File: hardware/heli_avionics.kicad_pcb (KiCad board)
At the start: 2 copper layers, 69 x 81.3 mm, 20 parts, among them J1 Pin_Header_2x3, J2 JST_PH_01x02, J3 JST_XH_01x02, J4 JST_XH_01x02, J5 JST_PH_01x03, J6 Battery JST, J7 JST_ZH_01x02, Q1 AO3400A, SW1 Reset, U1 ATmega4808-A, U2 nRF24L01P, U3 DRV8212, U4 DRV8212, U5 BMP390L, U6 TPS7A2030PDBV, Y1 16MHz

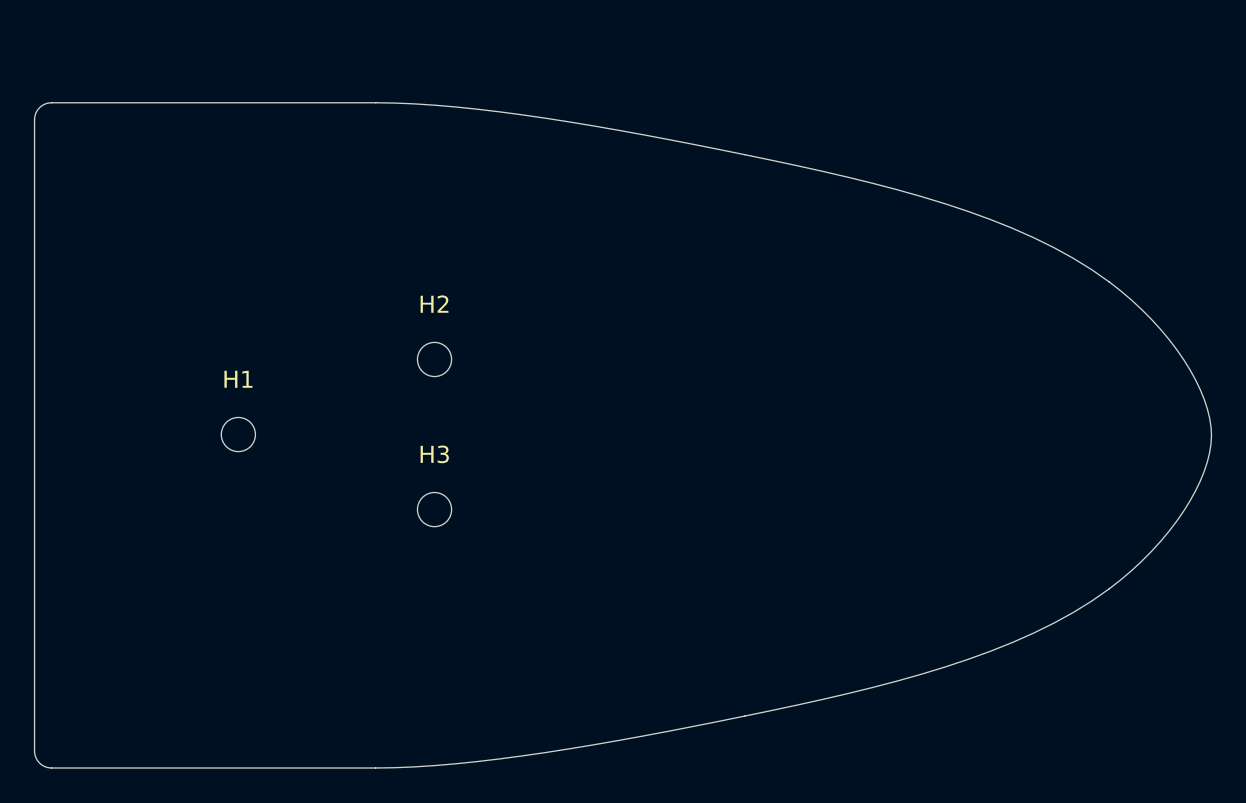
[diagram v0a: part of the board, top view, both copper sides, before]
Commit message: Update board outline and holes
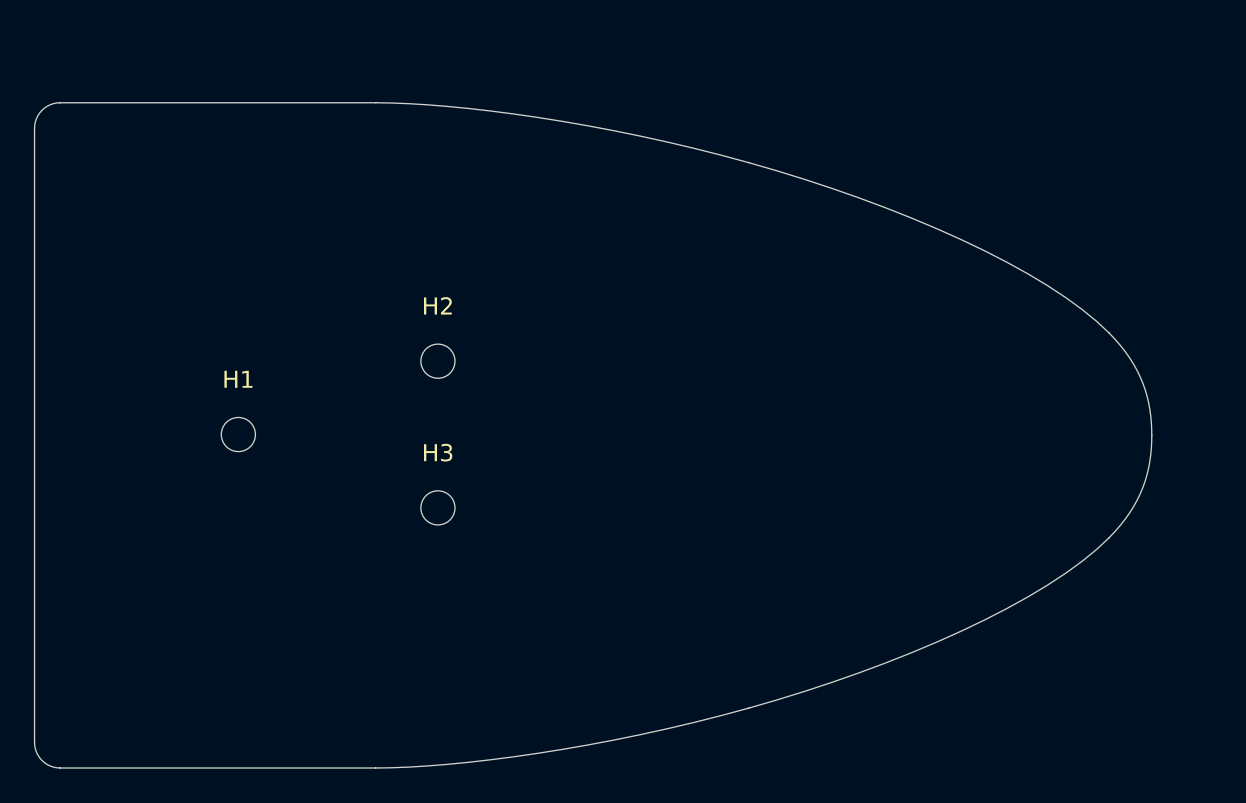
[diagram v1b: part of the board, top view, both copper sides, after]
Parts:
- moved H2 0.22 mm to (123.7, 115.2)
- moved H3 0.22 mm to (123.7, 123.8)
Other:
- board size 69 x 81.3 mm -> 65.5 x 81.3 mm
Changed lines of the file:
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@@
 	)
 	(footprint "MountingHole:MountingHole_2mm"
+		(locked yes)
 		(layer "F.Cu")
 		(at 112 119.5)
@@
 	)
 	(footprint "MountingHole:MountingHole_2mm"
+		(locked yes)
 		(layer "F.Cu")
-		(at 123.5 115.1)
+		(at 123.7 115.2)
 		(descr "Mounting Hole 2mm, no annular")
 		(tags "mounting hole 2mm no annular")
@@
 	)
 	(footprint "MountingHole:MountingHole_2mm"
+		(locked yes)
 		(layer "F.Cu")
-		(at 123.5 123.9)
+		(at 123.7 123.8)
 		(descr "Mounting Hole 2mm, no annular")
 		(tags "mounting hole 2mm no annular")
@@
 		)
 	)
-	(gr_curve
-		(pts
-			(xy 120.05 139.05) (xy 125.800886 139.05) (xy 133.766523 137.629931) (xy 141.688838 136.00577)
-		)
+	(gr_line
+		(start 101.55 139.05)
+		(end 120.05 139.05)
+		(locked yes)
 		(stroke
 			(width 0.05)
@@
 	)
 	(gr_line
-		(start 101.05 100.05)
+		(start 101.55 100.05)
 		(end 120.05 100.05)
+		(locked yes)
 		(stroke
 			(width 0.05)
@@
 		(layer "Edge.Cuts")
 	)
-	(gr_curve
-		(pts
-			(xy 141.688838 103.09423) (xy 149.750062 104.746867) (xy 157.766431 106.610816) (xy 163.05 110.55)
-		)
+	(gr_arc
+		(start 100.05 101.55)
+		(mid 100.48934 100.48934)
+		(end 101.55 100.05)
+		(locked yes)
 		(stroke
 			(width 0.05)
@@
 		(layer "Edge.Cuts")
 	)
-	(gr_line
-		(start 100.05 101.05)
-		(end 100.05 138.05)
+	(gr_curve
+		(pts
+			(xy 120.05 139.05) (xy 124.714182 139.05) (xy 133.376407 137.933608) (xy 141.925954 135.538563)
+		)
+		(locked yes)
 		(stroke
 			(width 0.05)
@@
 	)
 	(gr_arc
-		(start 100.05 101.05)
-		(mid 100.342893 100.342893)
-		(end 101.05 100.05)
+		(start 101.55 139.05)
+		(mid 100.48934 138.61066)
+		(end 100.05 137.55)
+		(locked yes)
 		(stroke
 			(width 0.05)
@@
 		(layer "Edge.Cuts")
 	)
-	(gr_arc
-		(start 101.05 139.05)
-		(mid 100.342893 138.757107)
-		(end 100.05 138.05)
+	(gr_curve
+		(pts
+			(xy 163.05 125.55) (xy 164.992423 123.587547) (xy 165.55 121.649375) (xy 165.55 119.55)
+		)
+		(locked yes)
 		(stroke
 			(width 0.05)
@@
 		(layer "Edge.Cuts")
 	)
-	(gr_line
-		(start 101.05 139.05)
-		(end 120.05 139.05)
+	(gr_curve
+		(pts
+			(xy 141.925954 103.561437) (xy 150.705967 106.021043) (xy 159.367145 109.829167) (xy 163.05 113.55)
+		)
+		(locked yes)
 		(stroke
 			(width 0.05)
@@
 	(gr_curve
 		(pts
-			(xy 141.688838 136.00577) (xy 149.750062 134.353133) (xy 157.766431 132.489184) (xy 163.05 128.55)
+			(xy 163.05 113.55) (xy 164.992423 115.512453) (xy 165.55 117.450625) (xy 165.55 119.55)
+		)
+		(locked yes)
+		(stroke
+			(width 0.05)
+			(type default)
 		)
+		(layer "Edge.Cuts")
+	)
+	(gr_line
+		(start 100.05 101.55)
+		(end 100.05 137.55)
+		(locked yes)
 		(stroke
 			(width 0.05)
@@
 	(gr_curve
 		(pts
-			(xy 163.05 128.55) (xy 166.703256 125.826301) (xy 169.05 122.110462) (xy 169.05 119.55)
+			(xy 120.05 100.05) (xy 124.714182 100.05) (xy 133.376407 101.166392) (xy 141.925954 103.561437)
 		)
+		(locked yes)
 		(stroke
 			(width 0.05)
@@
 	(gr_curve
 		(pts
-			(xy 163.05 110.55) (xy 166.703256 113.273699) (xy 169.05 116.989538) (xy 169.05 119.55)
+			(xy 141.925954 135.538563) (xy 150.705967 133.078957) (xy 159.367145 129.270833) (xy 163.05 125.55)
 		)
+		(locked yes)
 		(stroke
 			(width 0.05)
@@
 		(layer "Edge.Cuts")
 	)
-	(gr_curve
-		(pts
-			(xy 120.05 100.05) (xy 125.800886 100.05) (xy 133.766523 101.470069) (xy 141.688838 103.09423)
-		)
-		(stroke
-			(width 0.05)
-			(type default)
-		)
-		(layer "Edge.Cuts")
-	)
 	(group ""
-		(members "16916c19-8b3e-481f-9ed7-a1829fcf8c76" "1a1f929f-24cc-4343-8b75-dc80babde140"
-			"2f680f45-36b3-43c4-b5d2-7d31df4e0a50" "539ec297-f601-4817-8122-52b44ec71d46"
-			"64959845-f969-4bb4-b8cc-bcd3a4d9321d" "6915b272-6e47-449c-b218-0eb0a2fffdb5"
-			"7bb54858-f2ce-4c33-9619-2467d5193030" "b0518644-9432-49e1-a8b0-c654bdb650f0"
-			"d0e3dfd3-48cd-4a07-a679-5c11b14ebc93" "dc3a4f89-0b61-4a27-83f4-05b7f5f67f68"
-			"fa338a06-17e0-49b6-9f95-3b01b6da9347"
+		(locked yes)
+		(members "086b7960-f897-4d5b-bae9-2c5464810328" "1d5ea587-6a4e-4813-9e82-e848f2147706"
+			"2de732c8-e48b-41a8-b013-2a6bb9d7659e" "430c376f-c476-4823-b4dd-4427e543d07f"
+			"4e7c2f19-1b43-4200-90b7-520990fd837a" "7fc5d93f-593f-48f4-bc77-a3df9f6c0ba8"
+			"9aa89945-3765-48d0-96a7-1b0fea6c9041" "a6542110-92bc-46b5-a45c-e666c1f0478b"
+			"b0f37582-a4f6-4bc1-b6ad-3bb2ffcfd67d" "d5c53762-2aff-4cd1-85f8-dcb732b001a8"
+			"d93a6dbc-aed8-41e5-bc07-3d0901917520"
 		)
 	)

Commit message: tryout more layout ideas
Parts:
- added AE1: Antenna_Shield, Connector_Wire:SolderWire-0.5sqmm_1x01_D0.9mm_OD2.1mm, F.Cu at (161.7, 120.1)
- added C1: 100nF, Capacitor_SMD:C_0603_1608Metric_Pad1.08x0.95mm_HandSolder, F.Cu at (181.5, 110.3)
- added C10: 2.2nF, Capacitor_SMD:C_0603_1608Metric_Pad1.08x0.95mm_HandSolder, F.Cu at (192.2, 132.9)
- added C11: 13pF, Capacitor_SMD:C_0603_1608Metric_Pad1.08x0.95mm_HandSolder, F.Cu at (192.2, 135.4)
- added C12: 4.7pF, Capacitor_SMD:C_0603_1608Metric_Pad1.08x0.95mm_HandSolder, F.Cu at (192.2, 137.9)
- added C13: 1.5pF, Capacitor_SMD:C_0603_1608Metric_Pad1.08x0.95mm_HandSolder, F.Cu at (157.0, 120.0)
- added C14: 1pF, Capacitor_SMD:C_0603_1608Metric_Pad1.08x0.95mm_HandSolder, F.Cu at (157.9, 122.9)
- added C15: 100nF, Capacitor_SMD:C_0603_1608Metric_Pad1.08x0.95mm_HandSolder, F.Cu at (213.4, 110.3)
- added C16: 100nF, Capacitor_SMD:C_0603_1608Metric_Pad1.08x0.95mm_HandSolder, F.Cu at (213.4, 112.8)
- added C17: 100nF, Capacitor_SMD:C_0603_1608Metric_Pad1.08x0.95mm_HandSolder, F.Cu at (213.4, 115.3)
- added C18: 100nF, Capacitor_SMD:C_0603_1608Metric_Pad1.08x0.95mm_HandSolder, F.Cu at (213.4, 117.8)
- added C19: 100nF, Capacitor_SMD:C_0603_1608Metric_Pad1.08x0.95mm_HandSolder, F.Cu at (207.6, 132.9)
- added C2: 100nF, Capacitor_SMD:C_0603_1608Metric_Pad1.08x0.95mm_HandSolder, F.Cu at (181.5, 112.8)
- added C20: 100nF, Capacitor_SMD:C_0603_1608Metric_Pad1.08x0.95mm_HandSolder, F.Cu at (207.6, 135.4)
- added C21: 10uF, Capacitor_SMD:C_0603_1608Metric_Pad1.08x0.95mm_HandSolder, F.Cu at (194.3, 110.3)
- added C22: 10uF, Capacitor_SMD:C_0603_1608Metric_Pad1.08x0.95mm_HandSolder, F.Cu at (194.3, 112.8)
- added C23: 270uF, Capacitor_THT:CP_Radial_D6.3mm_P2.50mm, F.Cu at (107.0, 135.2)
- added C24: 680uF, Capacitor_THT:CP_Radial_D7.5mm_P2.50mm, F.Cu at (115.0, 105.7)
- added C25: 680uF, Capacitor_THT:CP_Radial_D7.5mm_P2.50mm, F.Cu at (112.0, 126.6)
- added C26: 10uF, Capacitor_SMD:C_0603_1608Metric_Pad1.08x0.95mm_HandSolder, F.Cu at (207.6, 137.9)
- added C27: 1nF, Capacitor_SMD:C_0603_1608Metric_Pad1.08x0.95mm_HandSolder, F.Cu at (192.2, 145.5)
- added C28: 100nF, Capacitor_SMD:C_0603_1608Metric_Pad1.08x0.95mm_HandSolder, F.Cu at (181.5, 117.8)
- added C29: 10uF, Capacitor_SMD:C_0603_1608Metric_Pad1.08x0.95mm_HandSolder, F.Cu at (181.5, 120.3)
- added C3: 100nF, Capacitor_SMD:C_0603_1608Metric_Pad1.08x0.95mm_HandSolder, F.Cu at (181.5, 115.3)
- added C30: 10uF, Capacitor_SMD:C_0603_1608Metric_Pad1.08x0.95mm_HandSolder, F.Cu at (194.3, 115.3)
- added C31: 10uF, Capacitor_SMD:C_0603_1608Metric_Pad1.08x0.95mm_HandSolder, F.Cu at (194.3, 117.8)
- added C4: 10uF, Capacitor_SMD:C_0603_1608Metric_Pad1.08x0.95mm_HandSolder, F.Cu at (187.9, 132.9)
- added C5: 100nF, Capacitor_SMD:C_0603_1608Metric_Pad1.08x0.95mm_HandSolder, F.Cu at (187.9, 135.4)
- added C6: 100nF, Capacitor_SMD:C_0603_1608Metric_Pad1.08x0.95mm_HandSolder, F.Cu at (187.9, 137.9)
- added C7: 33nF, Capacitor_SMD:C_0603_1608Metric_Pad1.08x0.95mm_HandSolder, F.Cu at (187.9, 140.4)
- added C8: 10nF, Capacitor_SMD:C_0603_1608Metric_Pad1.08x0.95mm_HandSolder, F.Cu at (187.9, 142.9)
- added C9: 13pF, Capacitor_SMD:C_0603_1608Metric_Pad1.08x0.95mm_HandSolder, F.Cu at (187.9, 145.5)
- added J8: Conn_01x01, Connector_Wire:SolderWire-1sqmm_1x01_D1.4mm_OD3.9mm, F.Cu at (128.7, 104.4)
- added L1: 2.7nH, Inductor_SMD:L_0603_1608Metric_Pad1.05x0.95mm_HandSolder, F.Cu at (196.6, 132.9)
- added L2: 8.2nH, Inductor_SMD:L_0603_1608Metric_Pad1.05x0.95mm_HandSolder, F.Cu at (196.6, 135.4)
- added L3: 3.9nH, Inductor_SMD:L_0603_1608Metric_Pad1.05x0.95mm_HandSolder, F.Cu at (153.2, 120.0)
- added R1: 33k, Resistor_SMD:R_0603_1608Metric_Pad0.98x0.95mm_HandSolder, F.Cu at (181.5, 122.8)
- added R10: 100R, Resistor_SMD:R_0603_1608Metric_Pad0.98x0.95mm_HandSolder, F.Cu at (119.2, 131.3)
- added R11: 470R, Resistor_SMD:R_0603_1608Metric_Pad0.98x0.95mm_HandSolder, F.Cu at (181.5, 132.9)
- added R2: 330R, Resistor_SMD:R_0603_1608Metric_Pad0.98x0.95mm_HandSolder, F.Cu at (181.5, 125.3)
- added R3: 22k, Resistor_SMD:R_0603_1608Metric_Pad0.98x0.95mm_HandSolder, F.Cu at (196.6, 140.4)
- added R4: 1M, Resistor_SMD:R_0603_1608Metric_Pad0.98x0.95mm_HandSolder, F.Cu at (196.6, 142.9)
- added R5: 22k, Resistor_SMD:R_0603_1608Metric_Pad0.98x0.95mm_HandSolder, F.Cu at (194.3, 120.3)
- added R6: 22k, Resistor_SMD:R_0603_1608Metric_Pad0.98x0.95mm_HandSolder, F.Cu at (194.3, 122.8)
- added R7: 150R, Resistor_SMD:R_0603_1608Metric_Pad0.98x0.95mm_HandSolder, F.Cu at (194.3, 125.3)
- added R8: 51k, Resistor_SMD:R_0603_1608Metric_Pad0.98x0.95mm_HandSolder, F.Cu at (194.3, 127.9)
- added R9: 68R, Resistor_SMD:R_0603_1608Metric_Pad0.98x0.95mm_HandSolder, F.Cu at (181.5, 127.9)
- added TP1: TestPoint, TestPoint:TestPoint_Pad_1.5x1.5mm, F.Cu at (198.3, 110.8)
- added TP2: TestPoint, TestPoint:TestPoint_Pad_1.5x1.5mm, F.Cu at (198.3, 114.4)
- added TP3: TestPoint, TestPoint:TestPoint_Pad_1.5x1.5mm, F.Cu at (198.3, 117.9)
- added TP4: TestPoint, TestPoint:TestPoint_Pad_D1.5mm, F.Cu at (134.4, 104.7)
- added TP5: TestPoint, TestPoint:TestPoint_Keystone_5019_Minature, F.Cu at (140.2, 106.0)
- added U7: TPS7A2030PDBV, Package_TO_SOT_SMD:SOT-23-5_HandSoldering, F.Cu at (142.4, 110.5)
- J6: value Battery JST -> Conn_01x01; footprint Connector_Wire:SolderWire-1sqmm_1x02_P7.8mm_D1.4mm_OD3.9mm -> Connector_Wire:SolderWire-1sqmm_1x01_D1.4mm_OD3.9mm
- moved Y1 58.9 mm to (149.6, 127.0)
- moved U2 58.6 mm to (148.2, 119.9)
- moved J7 53.7 mm to (117.2, 135.6)
- moved U5 53.1 mm to (141.5, 118.3)
- moved U6 52.7 mm to (118.5, 112.2)
- moved Q1 52.3 mm to (124.5, 130.9)
- moved U4 51.9 mm to (111.7, 113.5)
- moved U3 51.3 mm to (112.5, 133.5)
- moved SW1 50.1 mm to (131.1, 134.2)
- moved J3 49.4 mm to (104.8, 112.0)
- moved J4 48.2 mm to (104.6, 120.9)
- moved J5 47.7 mm to (129.6, 109.7)
- moved U1 47.7 mm to (134.0, 119.8)
- moved D2 47.0 mm to (132.8, 127.9)
- moved J2 46.8 mm to (104.2, 128.9)
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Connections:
- net Net-(J5-Pin_2) renamed /Power circuits/VREG_EN
- J5 pad 1: +BATT -> GND
- J5 pad 3: GND -> +BATT
- J7 pad 1: GND -> Net-(J7-Pin_1)
- J7 pad 2: Net-(J7-Pin_2) -> GND
- U2 pad 15: VCC -> +3V0
- U2 pad 18: VCC -> +3V0
- U2 pad 7: VCC -> +3V0
- U3 pad 2: Net-(J2-Pin_1) -> Net-(J2-Pin_2)
- U3 pad 3: Net-(J2-Pin_2) -> Net-(J2-Pin_1)
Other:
- board size 65.5 x 81.3 mm -> 65.5 x 39 mm

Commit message: Setup board properties and design constraints
Also added some default trace and via sizes
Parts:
- removed C26, C29: 10uF, Capacitor_SMD:C_0603_1608Metric_Pad1.08x0.95mm_HandSolder
- C1, C15, C16, C17, C18, C19, C2, C20, C5, C6: value 100nF -> 22uF
- C21, C22, C30, C31, C4: value 10uF -> 22uF
- moved C18 53.9 mm to (163.3, 97.9)
- moved C16 53.1 mm to (163.3, 95.4)
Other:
- copper layers 2 -> 4

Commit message: Layout savepoint 1
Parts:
- AE1: value Antenna_Shield -> Antenna
- moved R8 77.9 mm to (117.7, 114.0), turned to 180 degrees
- moved R7 73.2 mm to (121.5, 118.1), turned to 180 degrees
- moved R6 72.7 mm to (121.7, 119.6), turned to 180 degrees
- moved R5 66.8 mm to (128.0, 112.5)
- moved C3 57.3 mm to (126.2, 130.3), turned to 90 degrees
- moved R3 54.1 mm to (148.7, 115.3), turned to 180 degrees
- moved C28 53.4 mm to (130.0, 131.8)
- moved R11 52.2 mm to (129.5, 128.3), turned to 180 degrees
- moved R4 52.0 mm to (148.3, 123.4), turned to 180 degrees
- moved C7 50.6 mm to (143.9, 115.3), turned to 180 degrees
- moved R2 49.2 mm to (133.3, 135.4), turned to 90 degrees
- moved L2 49.0 mm to (150.1, 119.9), turned to -90 degrees
- moved L1 45.8 mm to (152.1, 121.9), turned to -90 degrees
- moved R1 45.2 mm to (137.9, 134.9)
- moved C9 42.2 mm to (148.6, 130.0), turned to 180 degrees
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
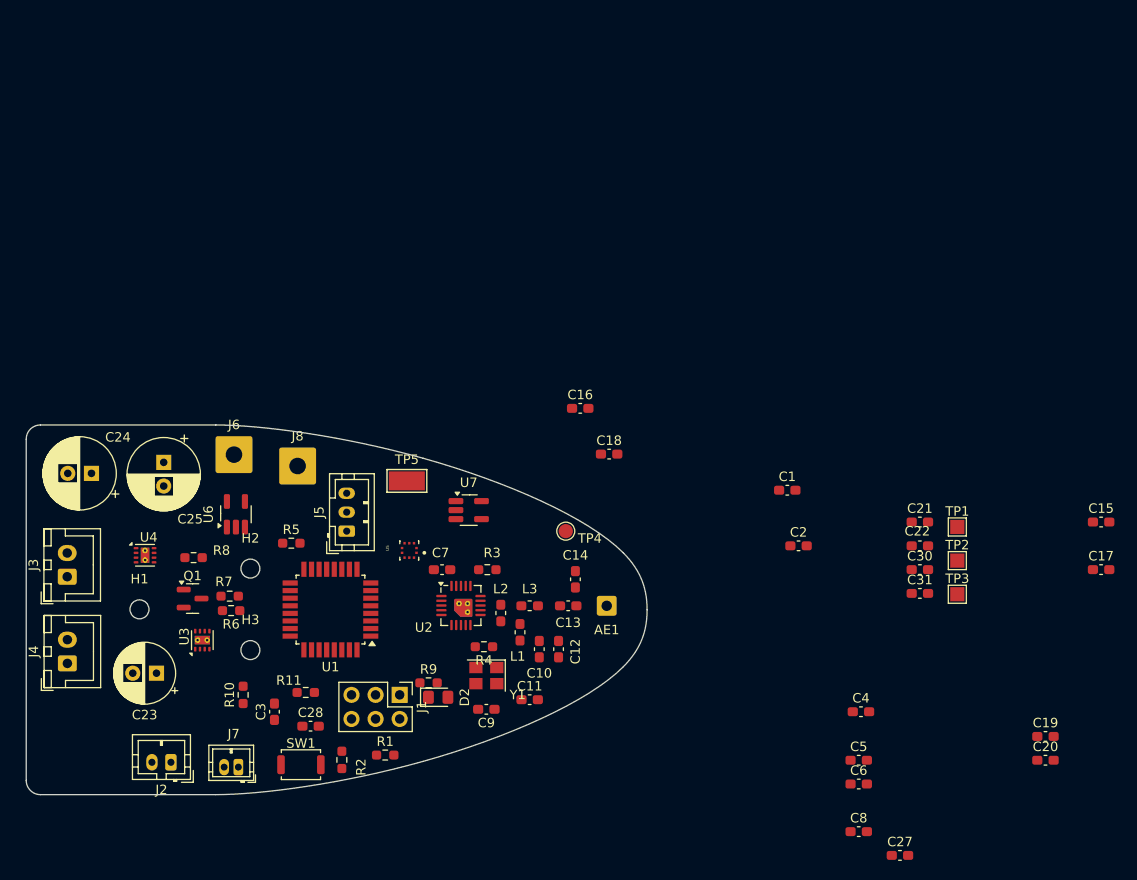
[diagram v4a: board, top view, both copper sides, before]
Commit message: New layout idea, savepoint
Me reckons this is the way to go. Only 1 motor bulk capacitor
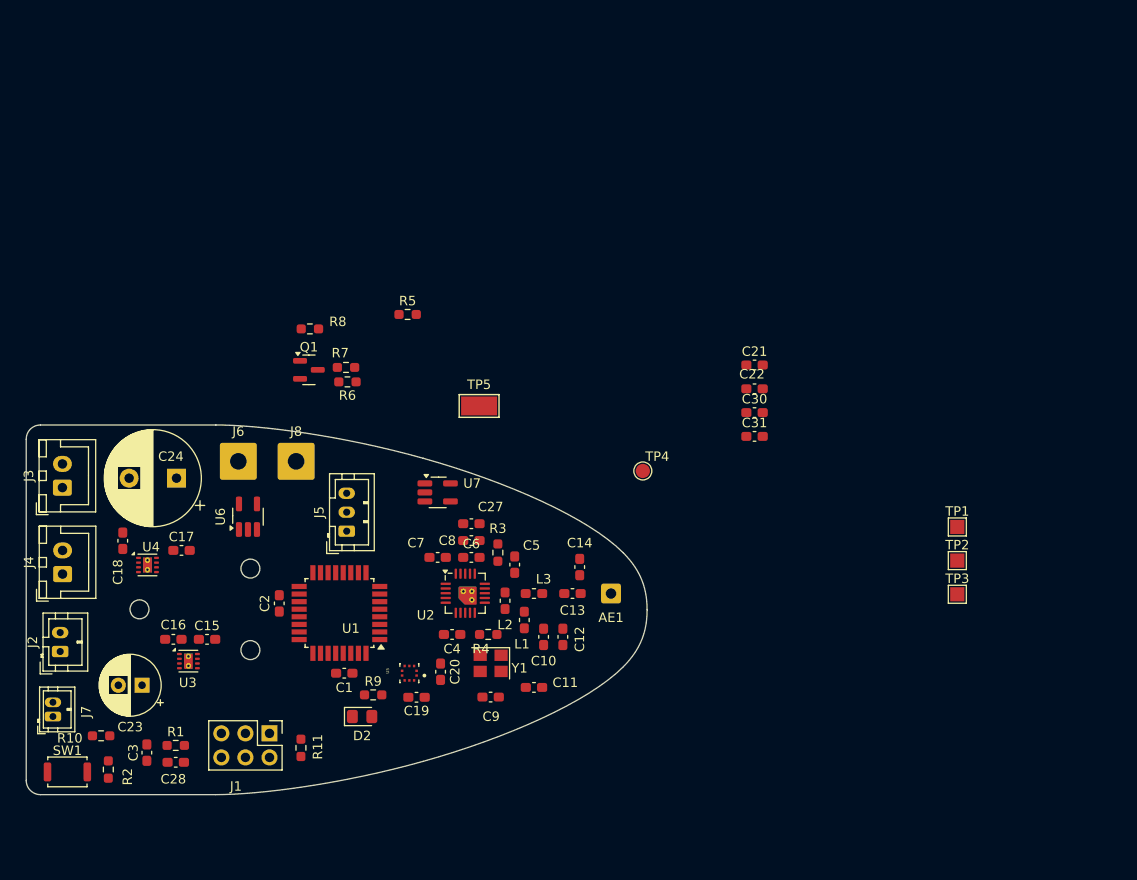
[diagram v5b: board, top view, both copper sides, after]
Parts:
- removed C25: 680uF, Capacitor_THT:CP_Radial_D7.5mm_P2.50mm
- C24: value 680uF -> 1500uF; footprint Capacitor_THT:CP_Radial_D7.5mm_P2.50mm -> Capacitor_THT:CP_Radial_D10.0mm_P5.00mm
- moved C17 97.0 mm to (116.4, 113.3)
- moved C15 95.1 mm to (119.1, 122.7)
- moved C19 66.5 mm to (141.2, 128.8), turned to 180 degrees
- moved C20 64.5 mm to (143.8, 126.1), turned to 90 degrees
- moved C27 57.2 mm to (147.0, 110.5)
- moved C2 55.1 mm to (126.7, 118.9), turned to -90 degrees
- moved C18 52.1 mm to (110.2, 112.3), turned to 90 degrees
- moved C8 51.1 mm to (147.0, 112.2)
- moved C1 50.6 mm to (133.6, 126.2)
- moved C16 49.4 mm to (115.6, 122.7), turned to 180 degrees
- moved C6 47.3 mm to (147.0, 114.0)
- moved C4 43.9 mm to (145.0, 122.2), turned to 180 degrees
- moved C5 41.8 mm to (151.6, 114.8), turned to 90 degrees
- moved Q1 27.1 mm to (129.9, 94.2)
- moved R5 27.1 mm to (140.3, 88.4)
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
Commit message: Layout update
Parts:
- moved C21 58.2 mm to (120.9, 109.7), turned to -90 degrees
- moved C22 53.1 mm to (127.0, 114.3), turned to -90 degrees
- moved TP3 51.5 mm to (147.8, 107.4)
- moved TP1 44.2 mm to (156.7, 95.8)
- moved TP2 44.2 mm to (156.7, 99.3)
- moved C30 40.7 mm to (136.8, 105.7), turned to 180 degrees
- moved C31 36.6 mm to (140.5, 104.6), turned to 180 degrees
- moved R8 28.7 mm to (141.2, 116.3), turned to 90 degrees
- moved R7 21.8 mm to (138.4, 115.3), turned to 0 degrees
- moved R5 21.6 mm to (135.6, 109.5), turned to -90 degrees
- moved Q1 21.0 mm to (140.7, 112.3), turned to 180 degrees
- moved R6 17.2 mm to (136.4, 112.5), turned to 0 degrees
- moved TP4 14.3 mm to (150.9, 103.1)
- moved J3 9.38 mm to (104.1, 116.0)
- moved J4 9.12 mm to (103.9, 106.7)
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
